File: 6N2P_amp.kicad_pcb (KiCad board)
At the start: 2 copper layers, 33 parts, among them J1 6.3MMTRSSwitched, U1 ECC83, U2 ECC83

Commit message: snap, ... started experimental routing
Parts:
- added C14: 470p, Capacitor_THT:C_Rect_L9.0mm_W4.0mm_P7.50mm_MKT, F.Cu at (183.6, -53.8)
- added C15: 22n, Capacitor_THT:C_Rect_L9.0mm_W4.0mm_P7.50mm_MKT, F.Cu at (169.1, -39.3)
- added C16: 10n, Capacitor_THT:C_Rect_L9.0mm_W4.0mm_P7.50mm_MKT, F.Cu at (183.6, -59.4)
- added J2: 6.3MMTRSSwitched, micha_custom:Reichelt_EBS63P, F.Cu at (54.0, 71.0)
- added J3: 6.3MMTRSSwitched, micha_custom:Reichelt_EBS63P, F.Cu at (80.0, 71.0)
- added J4: 6.3MMTRSSwitched, micha_custom:Reichelt_EBS63P, F.Cu at (229.0, 71.0)
- added R18: LDR03, OptoDevice:R_LDR_10x8.5mm_P7.6mm_Vertical, F.Cu at (157.8, -53.1)
- added R19: LDR03, OptoDevice:R_LDR_10x8.5mm_P7.6mm_Vertical, F.Cu at (157.8, -43.0)
- added R20: 56k, Resistor_THT:R_Axial_DIN0207_L6.3mm_D2.5mm_P10.16mm_Horizontal, F.Cu at (70.9, -23.9)
- added R21: LDR03, OptoDevice:R_LDR_10x8.5mm_P7.6mm_Vertical, F.Cu at (146.0, -30.0)
- added R22: LDR03, OptoDevice:R_LDR_10x8.5mm_P7.6mm_Vertical, F.Cu at (169.7, -47.1)
- added R23: LDR03, OptoDevice:R_LDR_10x8.5mm_P7.6mm_Vertical, F.Cu at (134.0, -30.0)
- added R24: LDR03, OptoDevice:R_LDR_10x8.5mm_P7.6mm_Vertical, F.Cu at (172.3, -57.1)
- added R25: 0R, Resistor_THT:R_Axial_DIN0204_L3.6mm_D1.6mm_P2.54mm_Vertical, F.Cu at (110.9, -22.3)
- added R26: DNP, Resistor_THT:R_Axial_DIN0204_L3.6mm_D1.6mm_P2.54mm_Vertical, F.Cu at (116.4, -22.3)
- added R27: 5.6k, Resistor_THT:R_Axial_DIN0207_L6.3mm_D2.5mm_P10.16mm_Horizontal, F.Cu at (84.2, -23.9)
- added R28: 470R/1W, Resistor_THT:R_Axial_DIN0207_L6.3mm_D2.5mm_P10.16mm_Horizontal, F.Cu at (97.5, -23.9)
- added R29: 0R, Resistor_THT:R_Axial_DIN0204_L3.6mm_D1.6mm_P2.54mm_Vertical, F.Cu at (122.0, -22.3)
- added R30: DNP, Resistor_THT:R_Axial_DIN0204_L3.6mm_D1.6mm_P2.54mm_Vertical, F.Cu at (127.6, -22.3)
- added R31: 8R/1W, Resistor_THT:R_Axial_DIN0207_L6.3mm_D2.5mm_P10.16mm_Horizontal, F.Cu at (158.4, -60.1)
- added R32: DNP, Resistor_THT:R_Axial_DIN0204_L3.6mm_D1.6mm_P2.54mm_Vertical, F.Cu at (133.2, -22.3)
- added R33: 0R, Resistor_THT:R_Axial_DIN0204_L3.6mm_D1.6mm_P2.54mm_Vertical, F.Cu at (62.0, -73.0)
- added RV1: 500k log, Potentiometer_THT:Potentiometer_Alps_RK163_Single_Horizontal, F.Cu at (98.8, 156.0)
- added RV10: 50k lin, Potentiometer_THT:Potentiometer_Alps_RK163_Single_Horizontal, F.Cu at (69.9, 184.1)
- added RV11: 1M log, Potentiometer_THT:Potentiometer_Alps_RK163_Single_Horizontal, F.Cu at (130.3, 184.1)
- added RV2: 500k log, Potentiometer_THT:Potentiometer_Alps_RK163_Single_Horizontal, F.Cu at (78.3, 156.0)
- added RV3: 250k lin, Potentiometer_THT:Potentiometer_Alps_RK163_Single_Horizontal, F.Cu at (158.8, 156.0)
- added RV4: 500k log, Potentiometer_THT:Potentiometer_Alps_RK163_Single_Horizontal, F.Cu at (58.9, 156.0)
- added RV5: 50k lin, Potentiometer_THT:Potentiometer_Alps_RK163_Single_Horizontal, F.Cu at (138.3, 156.0)
- added RV6: 1M log, Potentiometer_THT:Potentiometer_Alps_RK163_Single_Horizontal, F.Cu at (109.8, 184.1)
- added RV7: 500k log, Potentiometer_THT:Potentiometer_Alps_RK163_Single_Horizontal, F.Cu at (118.9, 156.0)
- added RV8: 250k lin, Potentiometer_THT:Potentiometer_Alps_RK163_Single_Horizontal, F.Cu at (89.3, 184.1)
- added RV9: 500k log, Potentiometer_THT:Potentiometer_Alps_RK163_Single_Horizontal, F.Cu at (150.8, 184.1)
- added TR1: VISATON_TR_10.16, micha_custom:VISATON_TR_10.16, F.Cu at (171.0, 82.0)
- added U3: 6N1P, w_vacuum:socket_gzc9-b, F.Cu at (166.7, 123.8)
- added U4: DSN-MINI-360, micha_custom:DSN-MINI-360, F.Cu at (71.6, 102.7)
- added U5: DSN-MINI-360, micha_custom:DSN-MINI-360, F.Cu at (109.7, 102.7)
- added U6: DSN-MINI-360, micha_custom:DSN-MINI-360, F.Cu at (188.3, 123.8)
- added U7: NCH6100HV, micha_custom:NCH6100HV, F.Cu at (243.0, 96.0)
- moved C1 300.6 mm to (16.6, -106.8)
- moved C10 300.6 mm to (5.98, -108.3)
- moved C11 300.6 mm to (16.6, -117.9)
- moved C12 300.6 mm to (16.6, -112.3)
- moved C13 300.6 mm to (27.3, -117.9)
- moved C2 300.6 mm to (19.3, -123.4)
- moved C3 300.6 mm to (5.98, -119.4)
- moved C4 300.6 mm to (5.98, -113.8)
- moved C5 300.6 mm to (20.9, -132.9)
- moved R10 300.6 mm to (-7.33, -116.1)
- moved R11 300.6 mm to (17.0, -137.7)
- moved R12 300.6 mm to (5.98, -124.2)
- moved R14 300.6 mm to (-7.33, -112.0)
- moved R15 300.6 mm to (-5.68, -128.2)
- moved R4 300.6 mm to (-7.33, -124.2)
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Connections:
- net Net-(C6-Pad1) renamed /HV_C
- net Net-(C7-Pad1) renamed /HV_B
- net Net-(C8-Pad1) renamed /HV_A
- net Net-(C9-Pad1) renamed /HV_in
- U1 pad 5: Net-(U1-Pad5) -> /6.3V_U1
- U1 pad 9: Net-(U1-Pad9) -> GND
- U2 pad 2: Net-(R15-Pad2) -> Net-(R23-Pad1)
- U2 pad 5: Net-(U2-Pad5) -> /6.3V_U2
- U2 pad 9: Net-(U2-Pad9) -> GND
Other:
- board outline added: 225 x 100 mm
- net class Default: clearance 0.2 -> 0.6; trace_width 0.25 -> 1; via_dia 0.8 -> 1; via_drill 0.4 -> 0.6
- rule trace_clearance: 0.2 -> 0.6

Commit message: snap
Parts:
- J1: value 6.3MMTRSSwitched -> guitar_in
- J2: value 6.3MMTRSSwitched -> speaker
- J3: value 6.3MMTRSSwitched -> fx_send
- J4: value 6.3MMTRSSwitched -> fx_return
- moved R1 273.7 mm to (45.0, 133.0), turned to 180 degrees
- moved R3 253.4 mm to (35.0, 95.0), turned to 270 degrees
- moved C1 224.2 mm to (30.0, 117.0), turned to 270 degrees
- moved C2 215.6 mm to (42.0, 91.0), turned to 270 degrees
- moved R28 169.5 mm to (151.0, 137.0), turned to 90 degrees
- moved J2 167.0 mm to (221.0, 71.0)
- moved R27 158.6 mm to (151.0, 120.0), turned to 90 degrees
- moved R31 157.6 mm to (236.0, 77.0), turned to 270 degrees
- moved J4 109.0 mm to (120.0, 71.0)
- moved RV6 55.2 mm to (138.8, 231.1)
- moved RV1 55.2 mm to (127.8, 203.0)
- moved RV10 55.2 mm to (98.9, 231.1)
- moved RV11 55.2 mm to (159.3, 231.1)
- moved RV2 55.2 mm to (107.3, 203.0)
- moved RV3 55.2 mm to (187.8, 203.0)
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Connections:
- net Net-(C2-Pad1) renamed /post_stage_1
- net Net-(C5-Pad2) renamed /clean_channel_bypass
- net Net-(J1-Pad1) renamed /guit_in
- net Net-(J2-Pad1) renamed /spkr_p
- net Net-(J2-Pad3) renamed /spkr_n
- net Net-(J3-Pad1) renamed /fx_send
- net Net-(J4-Pad1) renamed /fx_return
- net Net-(R15-Pad2) renamed /od_A
- net Net-(R27-Pad1) renamed /power_gate
- net Net-(R28-Pad2) renamed /power_cath
- net Net-(TR1-Pad1) renamed /power_anode
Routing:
- net GND: track 0.00 -> 93.0 mm
- net /spkr_n: track 0.00 -> 86.5 mm
- net /power_anode: track 0.00 -> 64.1 mm
- net /6.3V_U3: track 0.00 -> 34.1 mm
- net /spkr_p: track 0.00 -> 31.9 mm
- net /power_cath: track 0.00 -> 29.2 mm
- net /power_gate: track 0.00 -> 29.0 mm
- net Net-(J2-Pad4): track 0.00 -> 7.00 mm

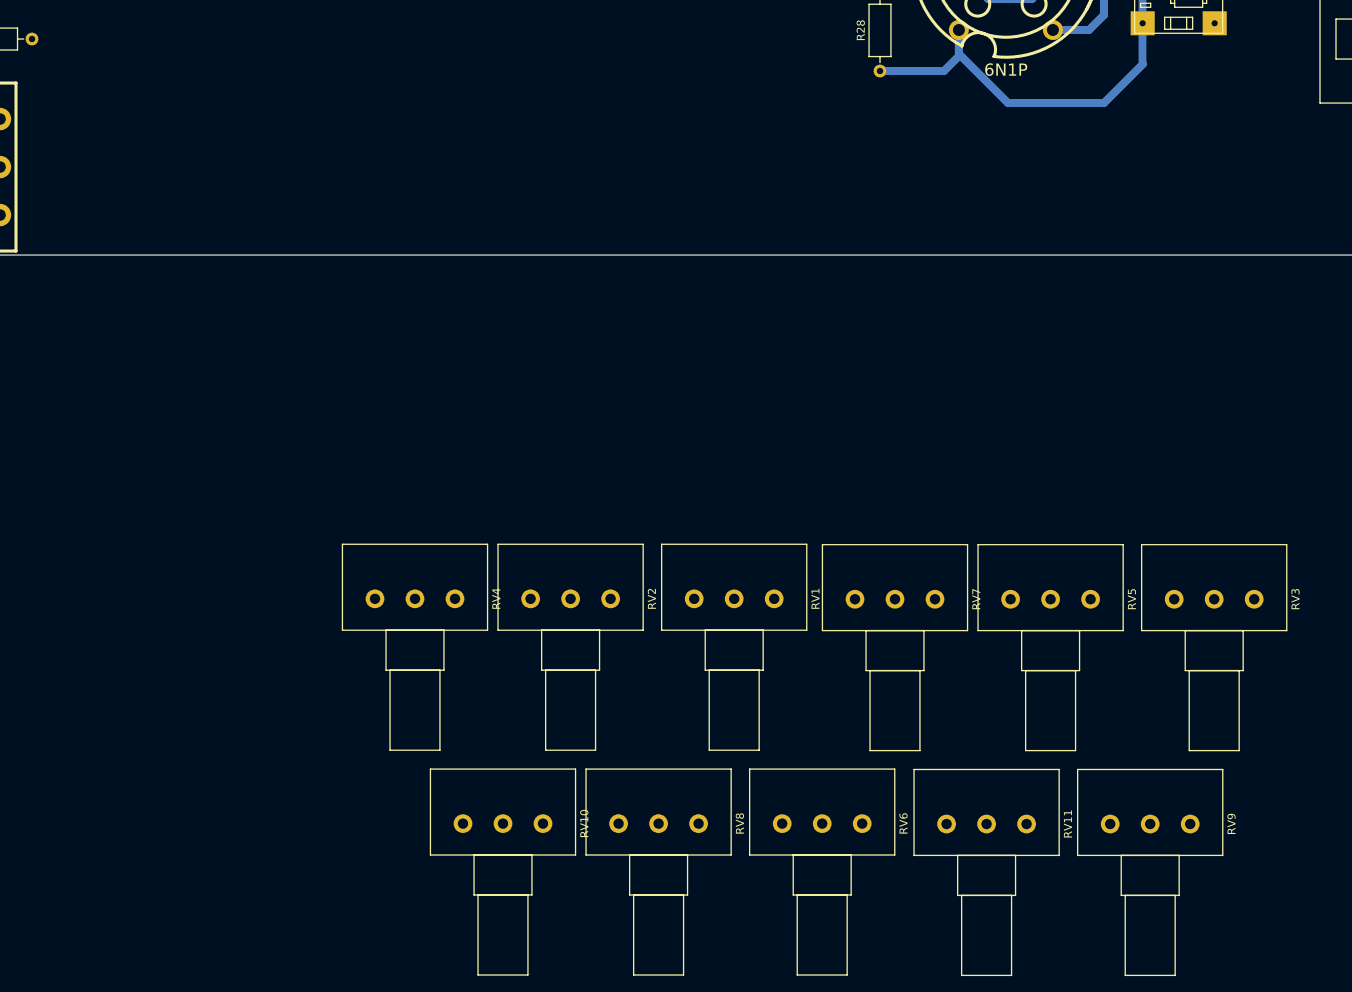
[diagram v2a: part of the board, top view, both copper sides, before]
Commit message: help text in layout
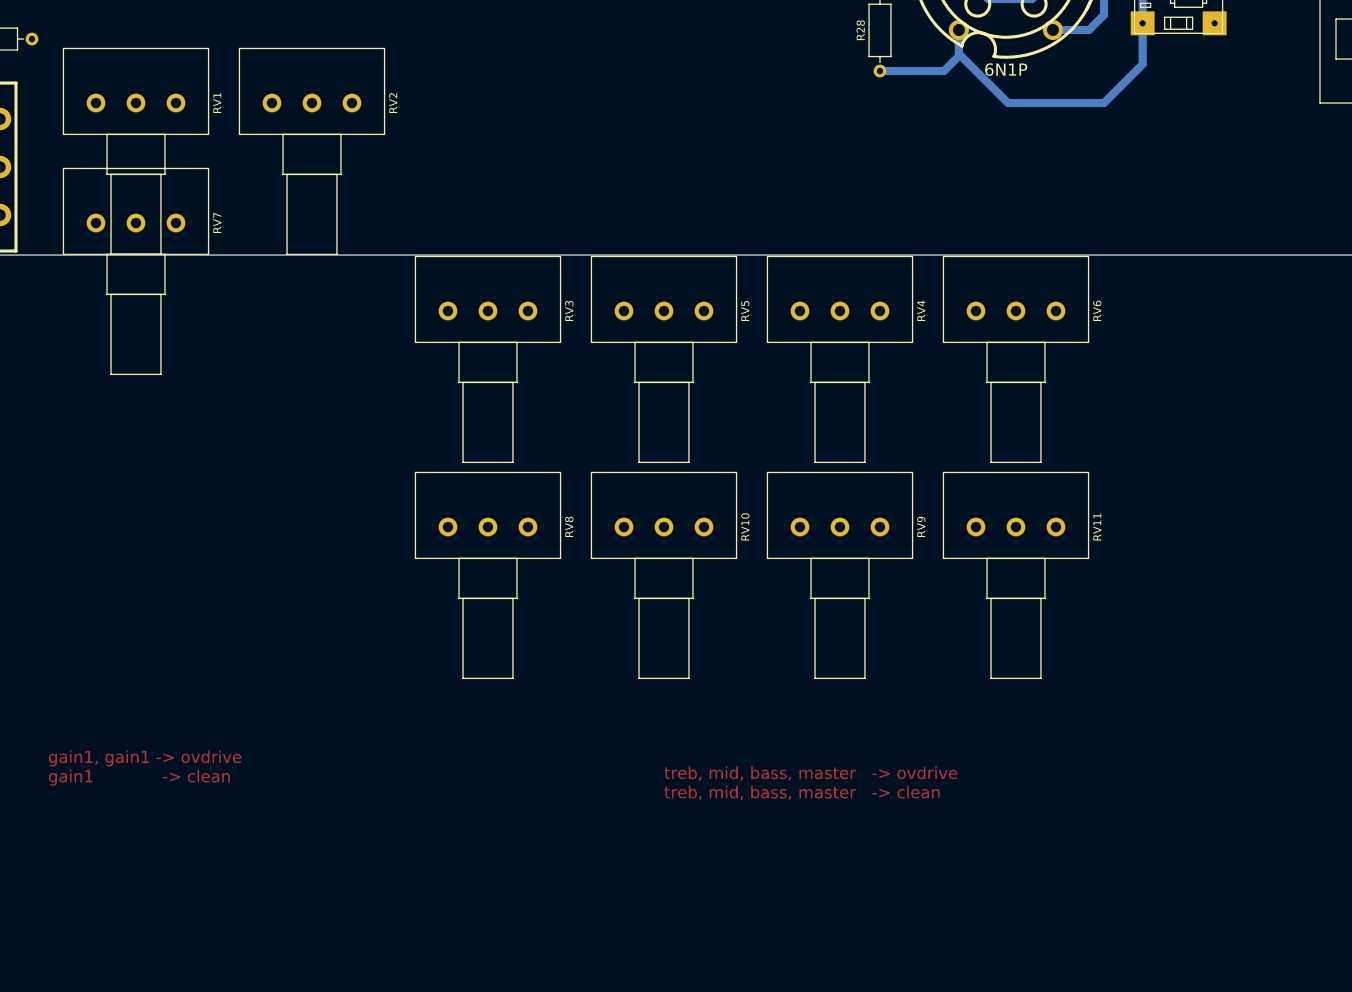
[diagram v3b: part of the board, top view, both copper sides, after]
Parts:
- moved RV7 105.9 mm to (53.0, 156.0)
- moved RV3 97.7 mm to (97.0, 167.0)
- moved RV1 97.1 mm to (53.0, 141.0)
- moved RV2 69.9 mm to (75.0, 141.0)
- moved RV6 68.5 mm to (163.0, 167.0)
- moved RV4 64.2 mm to (141.0, 167.0)
- moved RV5 60.3 mm to (119.0, 167.0)
- moved RV9 53.7 mm to (141.0, 194.0)
- moved RV8 42.8 mm to (97.0, 194.0)
- moved RV10 42.2 mm to (119.0, 194.0)
- moved RV11 37.3 mm to (163.0, 194.0)
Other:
- board text added: "gain1, gain1 -> ovdrive gain1 -> clean"
- board text added: "treb, mid, bass, master -> ovdrive treb, mid, bass, master -> clean"
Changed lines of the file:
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@@
   (general
     (thickness 1.6)
-    (drawings 9)
+    (drawings 11)
     (tracks 59)
     (zones 0)
@@
   )
   (module Potentiometer_THT:Potentiometer_Alps_RK163_Single_Horizontal (layer F.Cu)
-    (at 127.774999 202.975001 270)
+    (at 53 141 270)
     (descr "Potentiometer, horizontal, Alps RK163 Single, http://www.alps.com/prod/info/E/HTML/Potentiometer/RotaryPotentiometers/RK16/RK16_list.html")
     (tags "Potentiometer horizontal Alps RK163 Single")
@@
   )
   (module Potentiometer_THT:Potentiometer_Alps_RK163_Single_Horizontal (layer F.Cu)
-    (at 107.324999 202.975001 270)
+    (at 75 141 270)
     (descr "Potentiometer, horizontal, Alps RK163 Single, http://www.alps.com/prod/info/E/HTML/Potentiometer/RotaryPotentiometers/RK16/RK16_list.html")
     (tags "Potentiometer horizontal Alps RK163 Single")
@@
   )
   (module Potentiometer_THT:Potentiometer_Alps_RK163_Single_Horizontal (layer F.Cu)
-    (at 187.774999 203.025001 270)
+    (at 97 167 270)
     (descr "Potentiometer, horizontal, Alps RK163 Single, http://www.alps.com/prod/info/E/HTML/Potentiometer/RotaryPotentiometers/RK16/RK16_list.html")
     (tags "Potentiometer horizontal Alps RK163 Single")
@@
   )
   (module Potentiometer_THT:Potentiometer_Alps_RK163_Single_Horizontal (layer F.Cu)
-    (at 87.874999 202.975001 270)
+    (at 141 167 270)
     (descr "Potentiometer, horizontal, Alps RK163 Single, http://www.alps.com/prod/info/E/HTML/Potentiometer/RotaryPotentiometers/RK16/RK16_list.html")
     (tags "Potentiometer horizontal Alps RK163 Single")
@@
   )
   (module Potentiometer_THT:Potentiometer_Alps_RK163_Single_Horizontal (layer F.Cu)
-    (at 167.324999 203.025001 270)
+    (at 119 167 270)
     (descr "Potentiometer, horizontal, Alps RK163 Single, http://www.alps.com/prod/info/E/HTML/Potentiometer/RotaryPotentiometers/RK16/RK16_list.html")
     (tags "Potentiometer horizontal Alps RK163 Single")
@@
   )
   (module Potentiometer_THT:Potentiometer_Alps_RK163_Single_Horizontal (layer F.Cu)
-    (at 138.774999 231.075001 270)
+    (at 163 167 270)
     (descr "Potentiometer, horizontal, Alps RK163 Single, http://www.alps.com/prod/info/E/HTML/Potentiometer/RotaryPotentiometers/RK16/RK16_list.html")
     (tags "Potentiometer horizontal Alps RK163 Single")
@@
   )
   (module Potentiometer_THT:Potentiometer_Alps_RK163_Single_Horizontal (layer F.Cu)
-    (at 147.874999 203.025001 270)
+    (at 53 156 270)
     (descr "Potentiometer, horizontal, Alps RK163 Single, http://www.alps.com/prod/info/E/HTML/Potentiometer/RotaryPotentiometers/RK16/RK16_list.html")
     (tags "Potentiometer horizontal Alps RK163 Single")
@@
   )
   (module Potentiometer_THT:Potentiometer_Alps_RK163_Single_Horizontal (layer F.Cu)
-    (at 118.324999 231.075001 270)
+    (at 97 194 270)
     (descr "Potentiometer, horizontal, Alps RK163 Single, http://www.alps.com/prod/info/E/HTML/Potentiometer/RotaryPotentiometers/RK16/RK16_list.html")
     (tags "Potentiometer horizontal Alps RK163 Single")
@@
   )
   (module Potentiometer_THT:Potentiometer_Alps_RK163_Single_Horizontal (layer F.Cu)
-    (at 179.774999 231.125001 270)
+    (at 141 194 270)
     (descr "Potentiometer, horizontal, Alps RK163 Single, http://www.alps.com/prod/info/E/HTML/Potentiometer/RotaryPotentiometers/RK16/RK16_list.html")
     (tags "Potentiometer horizontal Alps RK163 Single")
@@
   )
   (module Potentiometer_THT:Potentiometer_Alps_RK163_Single_Horizontal (layer F.Cu)
-    (at 98.874999 231.075001 270)
+    (at 119 194 270)
     (descr "Potentiometer, horizontal, Alps RK163 Single, http://www.alps.com/prod/info/E/HTML/Potentiometer/RotaryPotentiometers/RK16/RK16_list.html")
     (tags "Potentiometer horizontal Alps RK163 Single")
@@
   )
   (module Potentiometer_THT:Potentiometer_Alps_RK163_Single_Horizontal (layer F.Cu)
-    (at 159.324999 231.125001 270)
+    (at 163 194 270)
     (descr "Potentiometer, horizontal, Alps RK163 Single, http://www.alps.com/prod/info/E/HTML/Potentiometer/RotaryPotentiometers/RK16/RK16_list.html")
     (tags "Potentiometer horizontal Alps RK163 Single")
@@
     )
   )
+  (gr_text "gain1, gain1 -> ovdrive\ngain1             -> clean" (at 47 224) (layer F.Cu)
+    (effects (font (size 1.5 1.5) (thickness 0.3)) (justify left))
+  )
+  (gr_text "treb, mid, bass, master   -> ovdrive\ntreb, mid, bass, master   -> clean" (at 124 226) (layer F.Cu)
+    (effects (font (size 1.5 1.5) (thickness 0.3)) (justify left))
+  )
   (gr_line (start 20 160) (end 20 60) (layer Edge.Cuts) (width 0.05))

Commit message: snap
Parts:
- R25, R29: value 0R -> ECC83
- R26, R30: value DNP -> 6N2P
- R32: value DNP -> ECCXX
- R33: value 0R -> 6N1P
- moved R5 276.6 mm to (49.0, 129.0)
- moved R4 254.7 mm to (65.0, 120.0), turned to 270 degrees
- moved C4 237.2 mm to (72.0, 114.0), turned to 90 degrees
- moved R6 234.4 mm to (67.0, 115.0), turned to 90 degrees
- moved R33 220.0 mm to (179.5, 113.0), turned to 180 degrees
- moved R32 136.7 mm to (171.5, 109.0)
- moved R25 131.2 mm to (58.5, 98.0)
- moved R26 129.6 mm to (68.0, 98.0), turned to 180 degrees
- moved R29 120.7 mm to (111.5, 98.0)
- moved R30 120.4 mm to (121.0, 98.0), turned to 180 degrees
- moved U4 7.00 mm to (83.0, 113.0)
- moved C2 5.00 mm to (39.0, 95.0)
- moved R3 3.61 mm to (32.0, 93.0)
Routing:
- net GND: track 93.0 -> 207.2 mm
- net /6.3V_U1: track 0.00 -> 45.1 mm
- net /6.3V_U2: track 0.00 -> 38.6 mm
- net Net-(C3-Pad1): track 0.00 -> 18.3 mm
- net Net-(C4-Pad1): track 0.00 -> 14.2 mm
- net Net-(R29-Pad2): track 0.00 -> 13.1 mm
- net Net-(R25-Pad2): track 0.00 -> 12.7 mm
- net Net-(R32-Pad2): track 0.00 -> 10.7 mm
- net /6.3V_U3: track 34.1 -> 33.4 mm

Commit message: added the ldr leds
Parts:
- added D1: LED, LED_THT:LED_D5.0mm, F.Cu at (51.0, 138.0)
- added D2: LED, LED_THT:LED_D5.0mm, F.Cu at (89.0, 141.0)
- added D3: LED, LED_THT:LED_D5.0mm, F.Cu at (135.5, 267.3)
- added D4: LED, LED_THT:LED_D5.0mm, F.Cu at (143.0, 267.3)
- added D5: LED, LED_THT:LED_D5.0mm, F.Cu at (135.5, 274.8)
- added D6: LED, LED_THT:LED_D5.0mm, F.Cu at (143.0, 274.8)
- moved C5 269.1 mm to (83.0, 129.0), turned to 180 degrees
- moved C3 250.0 mm to (71.0, 122.0), turned to 270 degrees
- moved R7 240.6 mm to (37.0, 98.0)
- moved R18 210.6 mm to (65.0, 136.0), turned to 270 degrees
- moved R19 196.8 mm to (76.0, 136.0), turned to 270 degrees
- moved RV7 38.0 mm to (53.0, 194.0)
- moved RV1 26.0 mm to (53.0, 167.0)
- moved RV2 26.0 mm to (75.0, 167.0)
- moved C2 16.1 mm to (37.0, 111.0), turned to 90 degrees
- moved R3 5.00 mm to (32.0, 98.0)
- moved R1 3.61 mm to (43.0, 130.0)
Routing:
- net GND: track 207.2 -> 269.4 mm
- net /clean_channel_bypass: track 0.00 -> 50.2 mm
- net /guit_in: track 0.00 -> 37.4 mm
- net Net-(C2-Pad2): track 0.00 -> 20.2 mm
- net Net-(C1-Pad1): track 0.00 -> 12.9 mm
- net Net-(C3-Pad1): track 18.3 -> 25.1 mm
- net Net-(C3-Pad2): track 0.00 -> 6.27 mm
- net /HV_C: track 0.00 -> 5.00 mm

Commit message: snap
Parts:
- moved R8 277.6 mm to (113.0, 130.0), turned to 180 degrees
- moved R9 276.8 mm to (117.0, 126.0), turned to 180 degrees
- moved R14 257.7 mm to (89.0, 127.0)
- moved C10 254.9 mm to (91.0, 132.0)
- moved R15 244.0 mm to (88.0, 97.0)
- moved R16 204.7 mm to (119.0, 112.0), turned to 90 degrees
- moved U5 3.00 mm to (132.0, 113.0)
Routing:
- net /HV_B: track 0.00 -> 34.3 mm
- net Net-(R8-Pad1): track 0.00 -> 29.0 mm
- net GND: track 269.4 -> 295.6 mm
- net Net-(C10-Pad1): track 0.00 -> 19.0 mm
- net /od_A: track 0.00 -> 7.93 mm
- net Net-(C11-Pad2): track 0.00 -> 6.94 mm
- net /6.3V_U2: track 38.6 -> 43.2 mm
